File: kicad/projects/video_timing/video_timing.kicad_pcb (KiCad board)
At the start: 2 copper layers, 203.2 x 97.8 mm, 52 parts, among them J1 peripheral_addr_bus_connector, J2 peripheral_aux_connector, J3 peripheral_membank_connector, J4 Conn_01x16_Socket, U1 74HC161, U10 74HC30, U11 74HC30, U12 74HC30, U13 74HC30, U14 74HC30, U15 74HC30, U16 74HC30, U17 74HC30, U18 74HC161, U2 74HC161, U20 74HC11, U21 74HC04, U3 74HC161, U4 74HC161, U5 74HC161, U6 74HC04, U7 74HC04, U8 74HC00, U9 74HC00, X1 CXO_DIP8

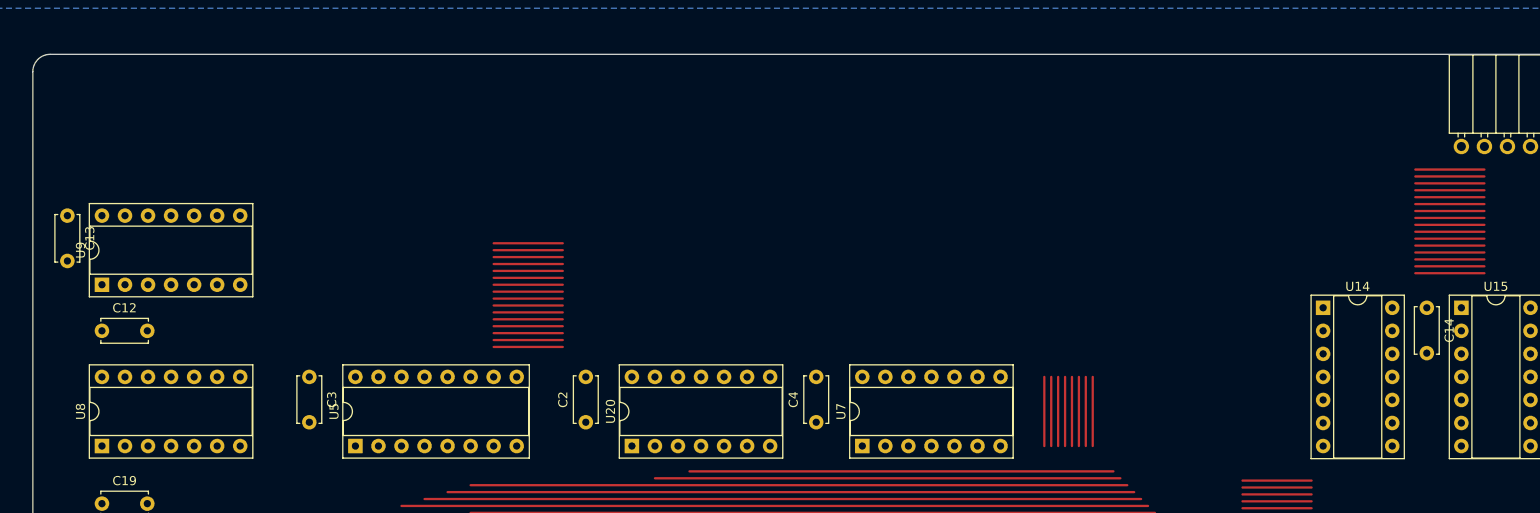
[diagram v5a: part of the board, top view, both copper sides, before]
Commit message: Adding video aux and some bits and bieces on video boards.
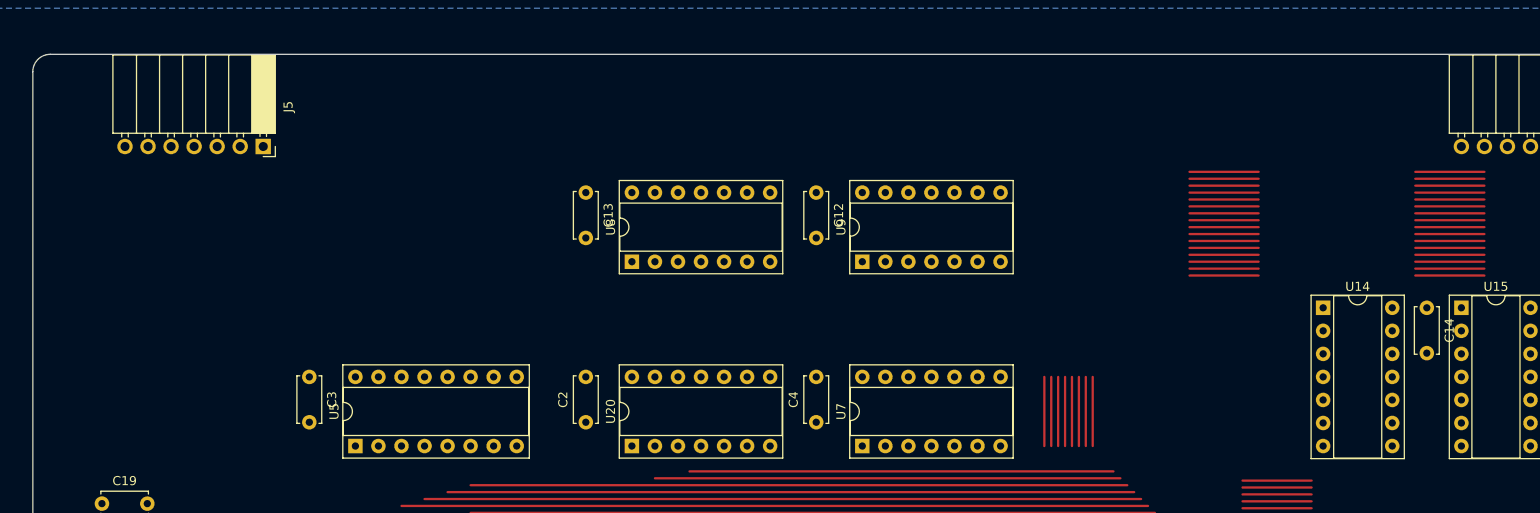
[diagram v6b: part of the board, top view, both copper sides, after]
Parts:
- added J5: video_aux, Connector_PinSocket_2.54mm:PinSocket_1x07_P2.54mm_Horizontal, F.Cu at (76.2, 61.0)
- moved U9 83.9 mm to (142.2, 73.7)
- moved C12 80.2 mm to (137.2, 66.0), turned to -90 degrees
- moved U8 61.9 mm to (116.8, 73.7)
- moved C13 57.2 mm to (111.8, 66.0)

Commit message: Start PCB for video timing.
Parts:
- added TP2: TestPoint, Connector_Pin:Pin_D1.0mm_L10.0mm, F.Cu at (58.4, 76.2)
- added TP3: TestPoint, Connector_Pin:Pin_D1.0mm_L10.0mm, F.Cu at (63.5, 77.0)
- added TP4: TestPoint, Connector_Pin:Pin_D1.0mm_L10.0mm, F.Cu at (68.1, 76.2)
- added TP5: TestPoint, Connector_Pin:Pin_D1.0mm_L10.0mm, F.Cu at (71.4, 76.5)
- added TP6: TestPoint, Connector_Pin:Pin_D1.0mm_L10.0mm, F.Cu at (74.7, 76.7)
- moved C17 6.35 mm to (246.4, 109.2), turned to 180 degrees
- moved C22 6.35 mm to (246.4, 73.7), turned to 180 degrees
- moved J5 2.54 mm to (73.7, 61.0)
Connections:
- TP1 pad 1: unconnected-(TP1-Pad1) -> /V_BLANK
- U6 pad 1: /PIXEL_CLOCK -> GND
- U6 pad 2: /~{PIXEL_CLOCK} -> unconnected-(U6-Pad2)
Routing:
- net VCC: track 0.00 -> 553.0 mm, vias 0 -> 5
- net /~{COL_INDEX_200}: track 0.00 -> 259.3 mm, vias 0 -> 3
- net /ROW_03: track 105.9 -> 325.3 mm, vias 0 -> 12
- net /ROW_02: track 101.6 -> 320.2 mm, vias 0 -> 8
- net /COL_07: track 65.8 -> 282.3 mm, vias 0 -> 4
- net /~{COL_00}: track 7.62 -> 214.5 mm, vias 0 -> 10
- net /COL_02: track 100.1 -> 294.6 mm, vias 0 -> 12
- net /~{COL_01}: track 7.62 -> 201.1 mm, vias 0 -> 9
- net /COL_03: track 96.8 -> 285.1 mm, vias 0 -> 12
- net /ROW_09: track 77.2 -> 259.6 mm, vias 0 -> 4
- net /COL_06: track 69.1 -> 244.7 mm, vias 0 -> 8
- net /COL_05: track 72.4 -> 242.9 mm, vias 0 -> 14
- net /ROW_08: track 81.8 -> 241.6 mm, vias 0 -> 11
- net /COL_04: track 75.7 -> 231.6 mm, vias 0 -> 10
- net /~{ROW_01}: track 7.62 -> 157.1 mm, vias 0 -> 6
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
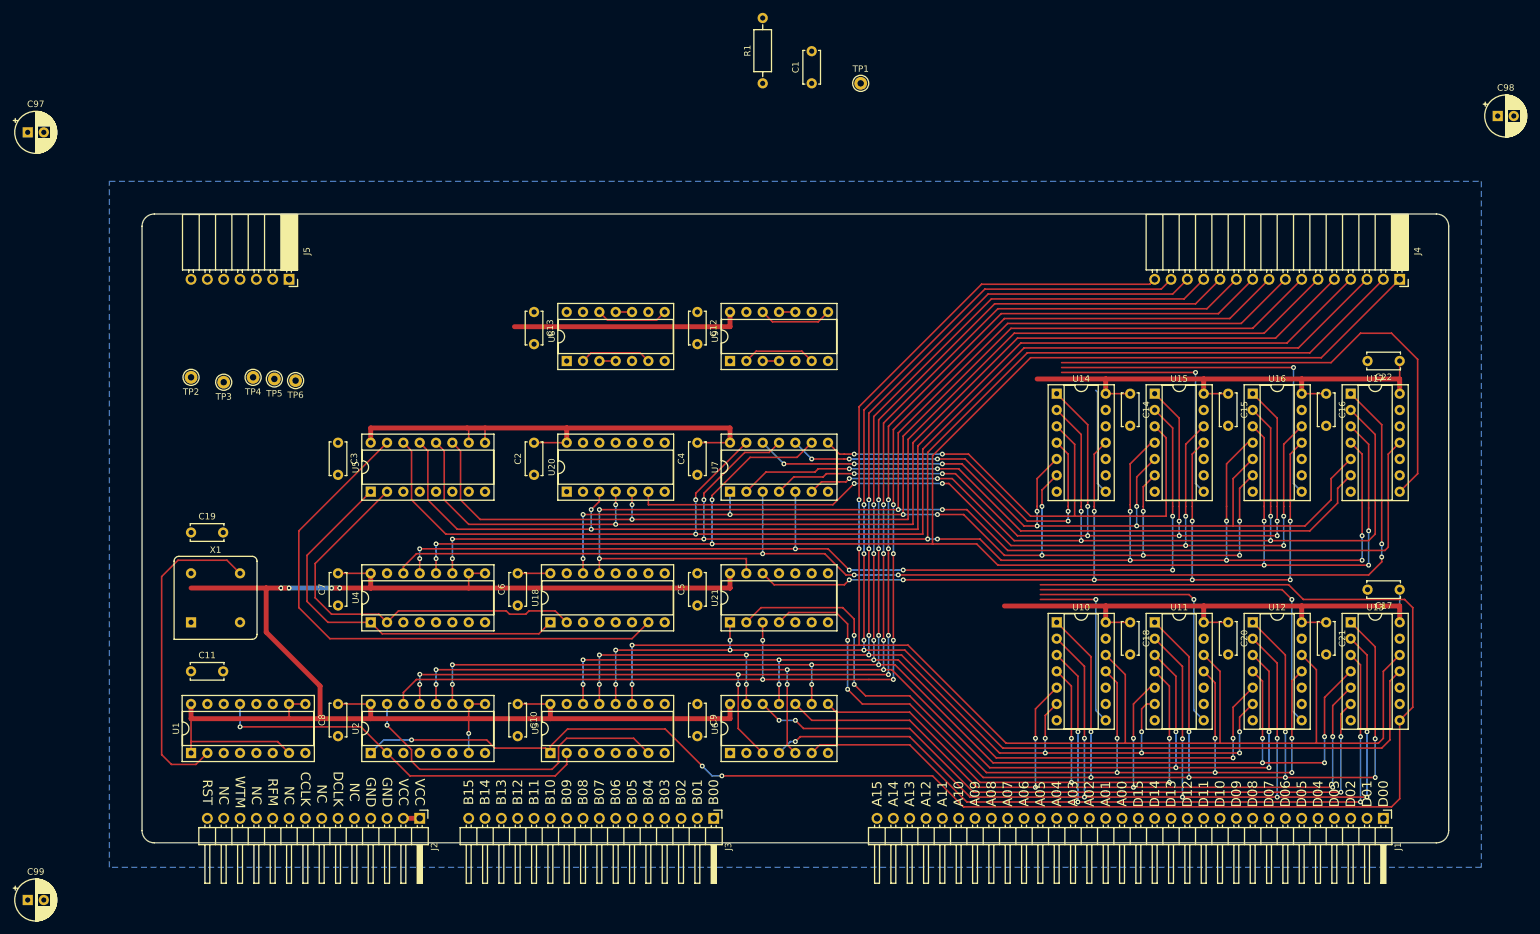
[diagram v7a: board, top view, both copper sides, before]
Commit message: Majority of video timing PCB layout done. Text and labels next.
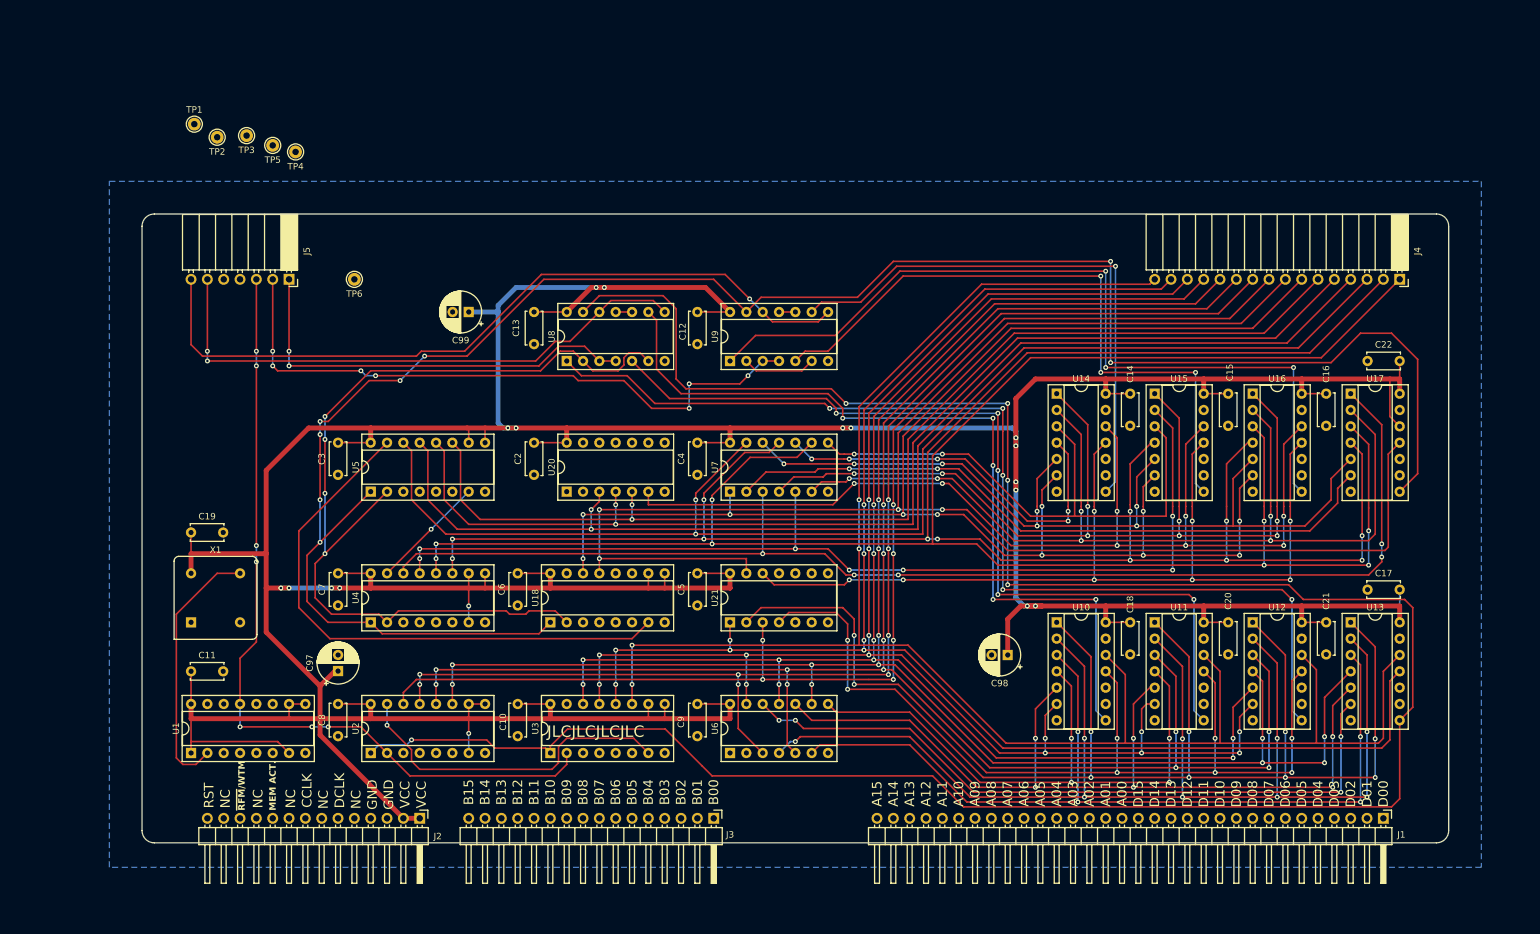
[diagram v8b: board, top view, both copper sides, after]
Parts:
- removed C1: C, Capacitor_THT:C_Disc_D5.0mm_W2.5mm_P5.00mm
- removed R1: R_US, Resistor_THT:R_Axial_DIN0207_L6.3mm_D2.5mm_P10.16mm_Horizontal
- moved C99 114.3 mm to (101.6, 66.0), turned to 180 degrees
- moved C98 113.3 mm to (185.4, 119.4), turned to 180 degrees
- moved TP1 103.8 mm to (58.9, 36.8)
- moved C97 96.7 mm to (81.3, 121.9), turned to 90 degrees
- moved TP3 38.5 mm to (67.1, 38.6)
- moved TP2 37.6 mm to (62.5, 38.9)
- moved TP5 36.3 mm to (71.1, 40.1)
- moved TP4 35.7 mm to (74.7, 41.1)
- moved TP6 18.2 mm to (83.8, 61.0)
- turned J2 to 0 degrees
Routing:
- net VCC: track 553.0 -> 809.4 mm, vias 5 -> 18
- net /~{ROW_INDEX_525}: track 142.5 -> 306.9 mm, vias 0 -> 8
- net /~{COL_INDEX_200}: track 259.3 -> 373.1 mm, vias 3 -> 5
- net /V_BLANK: track 11.4 -> 118.9 mm, vias 0 -> 1
- net /~{COL_INDEX_188}: track 59.2 -> 164.1 mm, vias 1 -> 5
- net /~{COL_INDEX_160}: track 28.3 -> 129.4 mm, vias 1 -> 5
- net /V_SYNC: track 2.54 -> 100.2 mm, vias 0 -> 7
- net /~{COL_INDEX_164}: track 43.6 -> 139.1 mm, vias 1 -> 5
- net /H_BLANK: track 11.2 -> 88.4 mm, vias 0 -> 2
- net /~{ROW_INDEX_492}: track 55.9 -> 128.2 mm, vias 1 -> 3
- net /~{ROW_INDEX_480}: track 16.4 -> 85.9 mm, vias 0 -> 1
- net /~{H_SYNC}: track 74.9 -> 143.2 mm, vias 0 -> 4
- net /PIXEL_CLOCK: track 60.0 -> 127.1 mm, vias 1 -> 7
- net /H_SYNC: track 2.54 -> 66.5 mm, vias 0 -> 2
- net /~{ROW_INDEX_490}: track 39.9 -> 101.8 mm, vias 1 -> 3
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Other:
- board text added: "JLCJLCJLCJLC"
